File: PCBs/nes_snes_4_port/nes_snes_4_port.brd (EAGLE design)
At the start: 62.2 x 40.9 mm, 24 parts, among them J1 RJ45, J2 RJ45, U1 74245, U2 MC74VHC1GT125, U3 MC74VHC1GT125, U4 MC74VHC1GT125, U5 MC74VHC1GT125

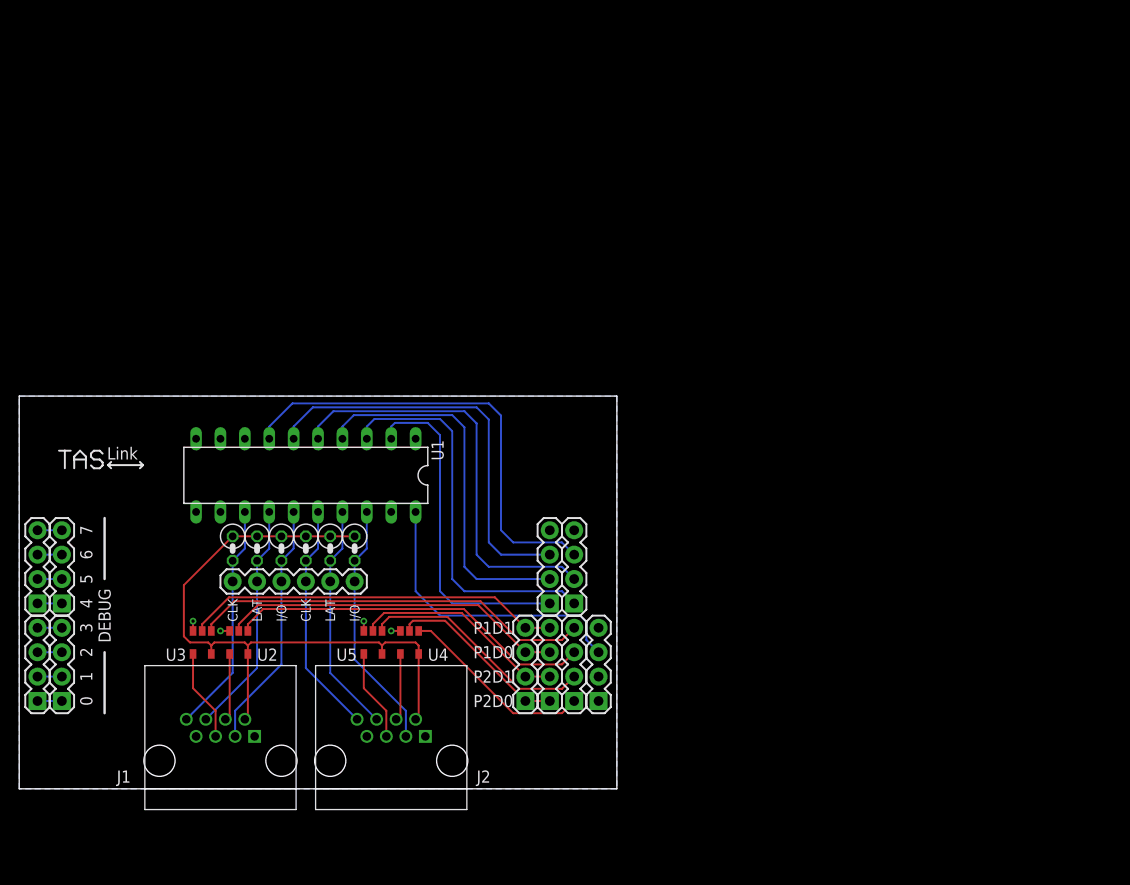
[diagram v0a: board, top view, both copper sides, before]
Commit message: Lots of work on the 4 port PCB. Added some shielded RJ45s to the library.
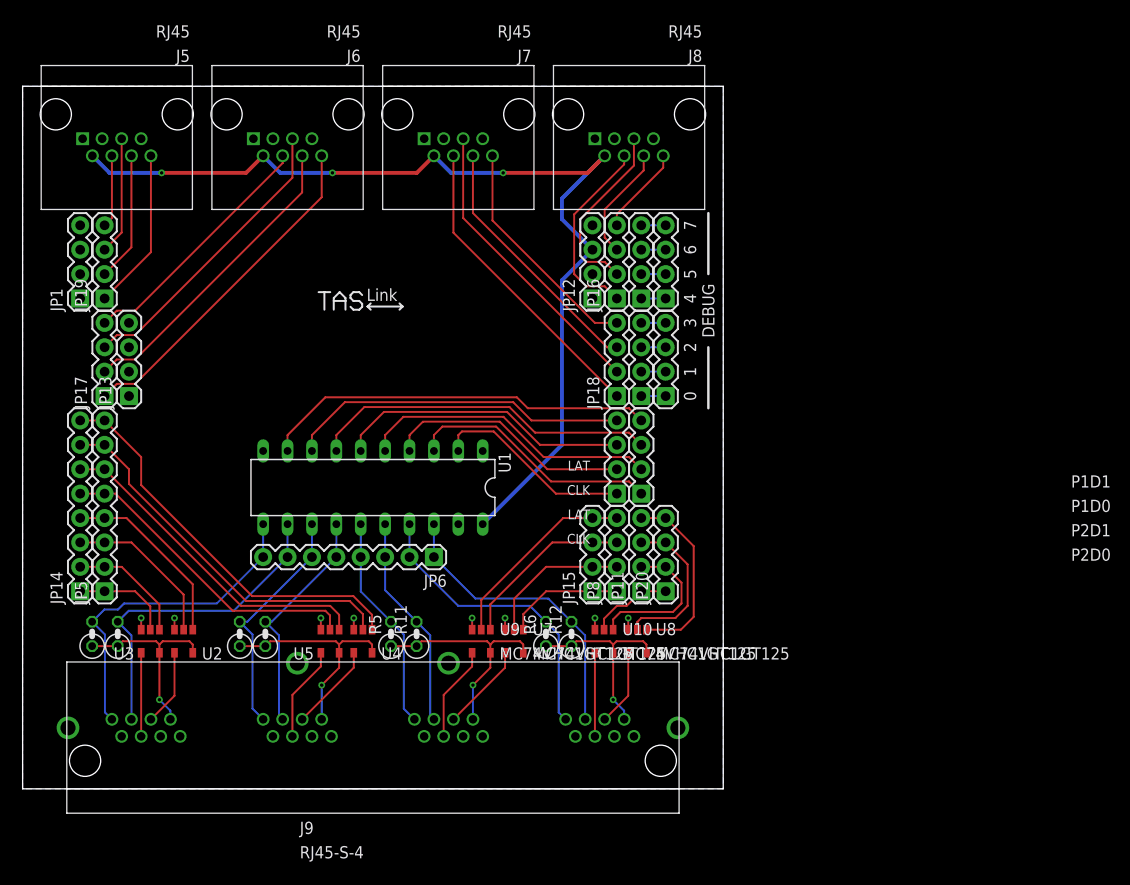
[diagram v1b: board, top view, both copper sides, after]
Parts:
- removed J1, J2: RJ45, TASLink:RJ45
- added J5, J6, J7, J8: RJ45, TASLink:RJ45
- added J9: RJ45-S-4, TASLink:RJ45-S-4
- added JP13, JP15, JP16, JP17, JP18, JP19, JP20: (no value), SparkFun-Connectors:1X04
- added JP14, JP6: (no value), SparkFun-Connectors:1X08
- added R11, R12: 3.6k, rcl:0207/2V
- added U10, U7, U8, U9: MC74VHC1GT125, TASLink:TSOP-5
- JP5: device SparkFun-Connectors:1X06 -> SparkFun-Connectors:1X08
- moved JP10 70.4 mm to (67.3, 51.1)
- moved JP3 70.4 mm to (64.8, 51.1)
- moved JP9 70.4 mm to (67.3, 40.9)
- moved JP2 70.4 mm to (64.8, 40.9)
- moved JP1 68.3 mm to (6.35, 51.1)
- moved JP12 42.1 mm to (59.7, 51.1)
- moved R6 21.8 mm to (54.8, 16.1), turned to 90 degrees
- moved R1 17.1 mm to (7.59, 16.1), turned to 90 degrees
- moved R3 17.0 mm to (10.3, 16.1), turned to 90 degrees
- moved JP8 14.9 mm to (62.2, 20.6)
- moved R5 14.5 mm to (38.7, 16.1), turned to 90 degrees
- moved JP4 13.4 mm to (64.8, 30.7)
- moved JP7 13.4 mm to (62.2, 30.7)
- moved JP11 13.4 mm to (64.8, 20.6)
- moved JP5 13.4 mm to (8.89, 20.6), turned to 90 degrees
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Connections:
- net P1_CLOCK_LV renamed CP2_CLOCK_LV
- net P1_IODATA_LV renamed CP3_CLOCK_LV
- net P1_LATCH_LV renamed CP2_LATCH_LV
- net P2_CLOCK_LV renamed CP3_LATCH_LV
- net P2_IODATA_LV renamed CP4_LATCH_LV
- net P2_LATCH_LV renamed CP4_CLOCK_LV
- removed net CONSOLE+5V: J1.2, J2.2, R1.1, R2.1, R3.1, R4.1, R5.1, R6.1, U2.P$5, U3.P$5, U4.P$5, U5.P$5
- removed net P1_CLOCK: J1.8, JP5.1, R1.2, U1.13
- removed net P1_D0: J1.4, U2.P$4
- removed net P1_D0_LV: JP12.3, JP8.3, U2.P$2
- removed net P1_D0_OE_LV: JP11.3, U2.P$1
- removed net P1_D1: J1.5, U3.P$4
- removed net P1_D1_LV: JP12.4, JP8.4, U3.P$2
- removed net P1_D1_OE_LV: JP11.4, U3.P$1
- removed net P1_IODATA: J1.3, JP5.3, R5.2, U1.15
- removed net P1_LATCH: J1.6, JP5.2, R3.2, U1.14
- removed net P2_CLOCK: J2.8, JP5.4, R2.2, U1.16
- removed net P2_D0: J2.4, U4.P$4
- removed net P2_D0_OE_LV: JP11.1, U4.P$1
- removed net P2_D1: J2.5, U5.P$4
- removed net P2_D1_LV: JP12.2, JP8.2, U5.P$2
- removed net P2_D1_OE_LV: JP11.2, U5.P$1
- removed net P2_DO_LV: JP12.1, JP8.1, U4.P$2
- removed net P2_IODATA: J2.3, JP5.6, R6.2, U1.18
- removed net P2_LATCH: J2.6, JP5.5, R4.2, U1.17
- new net CP1_+5V: J9.1-2, R1.1, R3.1, U2.P$5, U3.P$5
- new net CP1_CLOCK: J9.1-8, JP6.8, R1.2, U1.11
- new net CP1_CLOCK_LV: JP4.4, U1.9
- new net CP1_D0: J9.1-4, U2.P$4
- new net CP1_D0_LV: JP14.3, JP5.3, U2.P$2
- new net CP1_D0_OE_LV: JP14.4, JP5.4, U2.P$1
- new net CP1_D1: J9.1-5, U3.P$4
- new net CP1_D1_LV: JP14.1, JP5.1, U3.P$2
- new net CP1_D1_OE_LV: JP14.2, JP5.2, U3.P$1
- new net CP1_IODATA: J9.1-3
- new net CP1_LATCH: J9.1-6, JP6.7, R3.2, U1.12
- new net CP1_LATCH_LV: JP7.4, U1.8
- new net CP2_+5V: J9.2-2, R2.1, R4.1, U4.P$5, U5.P$5
- new net CP2_CLOCK: J9.2-8, JP6.6, R2.2, U1.13
- new net CP2_D0: J9.2-4, U4.P$4
- new net CP2_D0_OE_LV: JP14.8, JP5.8, U4.P$1
- new net CP2_D1: J9.2-5, U5.P$4
- new net CP2_D1_LV: JP14.5, JP5.5, U5.P$2
- new net CP2_D1_OE_LV: JP14.6, JP5.6, U5.P$1
- new net CP2_DO_LV: JP14.7, JP5.7, U4.P$2
- new net CP2_IODATA: J9.2-3
- new net CP2_LATCH: J9.2-6, JP6.5, R4.2, U1.14
- new net CP3_+5V: J9.3-2, R11.1, R5.1, U7.P$5, U9.P$5
- new net CP3_CLOCK: J9.3-8, JP6.4, R5.2, U1.15
- new net CP3_D0: J9.3-4, U7.P$4
- new net CP3_D0_LV: JP15.2, JP8.2, U7.P$2
- new net CP3_D0_OE_LV: JP15.1, JP8.1, U7.P$1
- new net CP3_D1: J9.3-5, U9.P$4
- new net CP3_D1_LV: JP15.4, JP8.4, U9.P$2
- new net CP3_D1_OE_LV: JP15.3, JP8.3, U9.P$1
- new net CP3_IODATA: J9.3-3
- new net CP3_LATCH: J9.3-6, JP6.3, R11.2, U1.16
- new net CP4_+5V: J9.4-2, R12.1, R6.1, U10.P$5, U8.P$5
- new net CP4_CLOCK: J9.4-8, JP6.2, R6.2, U1.17
- new net CP4_D0: J9.4-4, U8.P$4
- new net CP4_D0_OE_LV: JP11.4, JP20.4, U8.P$1
- new net CP4_D1: J9.4-5, U10.P$4
- new net CP4_D1_LV: JP11.1, JP20.1, U10.P$2
- new net CP4_D1_OE_LV: JP11.2, JP20.2, U10.P$1
- new net CP4_DO_LV: JP11.3, JP20.3, U8.P$2
- new net CP4_IODATA: J9.4-3
- new net CP4_LATCH: J9.4-6, JP6.1, R12.2, U1.18
- new net VP1_CLOCK: J5.8, JP19.1
- new net VP1_D0: J5.4, JP19.4
- new net VP1_D1: J5.5, JP19.3
- new net VP1_D2: J5.3
- new net VP1_D3: J5.7
- new net VP1_LATCH: J5.6, JP19.2
- new net VP2_CLOCK: J6.8, JP17.1
- new net VP2_D0: J6.4, JP17.4
- new net VP2_D1: J6.5, JP17.3
- new net VP2_D2: J6.3
- new net VP2_D3: J6.7
- new net VP2_LATCH: J6.6, JP17.2
- new net VP3_CLOCK: J7.8, JP18.4
- new net VP3_D0: J7.4, JP18.1
- new net VP3_D1: J7.5, JP18.2
- new net VP3_D2: J7.3
- new net VP3_D3: J7.7
- new net VP3_LATCH: J7.6, JP18.3
- new net VP4_CLOCK: J8.8, JP16.4
- new net VP4_D0: J8.4, JP16.1
- new net VP4_D1: J8.5, JP16.2
- new net VP4_D2: J8.3
- new net VP4_D3: J8.7
- new net VP4_LATCH: J8.6, JP16.3
- net +3V3: now also J5.2, J6.2, J7.2, J8.2, JP12.3; no longer JP1.3
- net GND: now also J5.1, J6.1, J7.1, J8.1, J9.1-1, J9.2-1, J9.3-1, J9.4-1, J9.S1, J9.S2, J9.S3, J9.S4, JP12.1, JP13.1, U10.P$3, U7.P$3, U8.P$3, U9.P$3; no longer J1.1, J2.1, U1.11, U1.12
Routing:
- net +3V3: track 31.1 -> 104.0 mm, vias 0 -> 3
- net CONSOLE+5V: track 68.2 -> 0.00 mm
- net CP2_D0_OE_LV: track 0.00 -> 42.0 mm
- net P1_D1_OE_LV: track 41.7 -> 0.00 mm
- net CP1_CLOCK_LV: track 0.00 -> 41.1 mm
- net P1_D1_LV: track 39.4 -> 0.00 mm
- net CP2_DO_LV: track 0.00 -> 39.3 mm
- net P1_D0_OE_LV: track 38.2 -> 0.00 mm
- net P1_D0_LV: track 35.9 -> 0.00 mm
- net CP1_LATCH_LV: track 0.00 -> 35.6 mm
- net VP2_CLOCK: track 0.00 -> 35.5 mm
- net CP1_CLOCK: track 0.00 -> 35.0 mm
- net CP2_D1_OE_LV: track 0.00 -> 34.8 mm
- net CP1_LATCH: track 0.00 -> 34.6 mm
- net CP2_D1_LV: track 0.00 -> 32.8 mm
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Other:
- board size 62.2 x 40.9 mm -> 72.9 x 73.2 mm
- board text removed: "I/O"

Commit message: Tweaks to the 4 port PCB.
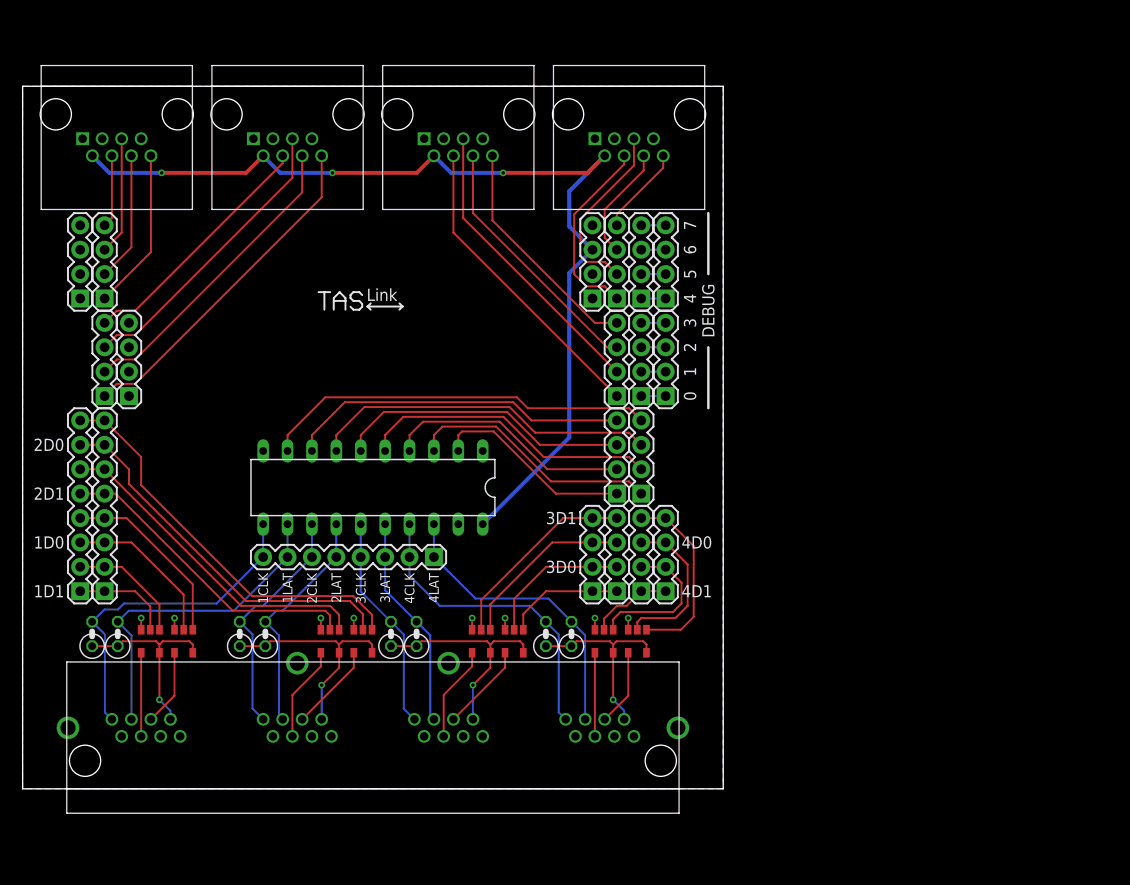
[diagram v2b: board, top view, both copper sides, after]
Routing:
- net CP4_CLOCK: track 31.4 -> 32.5 mm
- net +3V3: track 104.0 -> 103.4 mm
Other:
- board text added: "1CLK"
- board text added: "1D0"
- board text added: "1D1"
- board text added: "1LAT"
- board text added: "2CLK"
- board text added: "2D0"
- board text added: "2D1"
- board text added: "2LAT"
- board text added: "3CLK"
- board text added: "3D0"
- board text added: "3D1"
- board text added: "3LAT"
- board text added: "4CLK"
- board text added: "4D0"
- board text added: "4D1"
- board text added: "4LAT"
- board text removed: "CLK"
- board text removed: "LAT"
- board text removed: "P1D0"
- board text removed: "P1D1"
- board text removed: "P2D0"
- board text removed: "P2D1"
